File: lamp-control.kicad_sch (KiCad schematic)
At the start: 30 parts, among them J1 LED, J2 VIN, J3 Touch, J4 UART, J5 I²C, J6 SPI, Q1 BSS138, U1 ESP-12E, U2 AMS1117-3.3, U3 TTP223-BA6

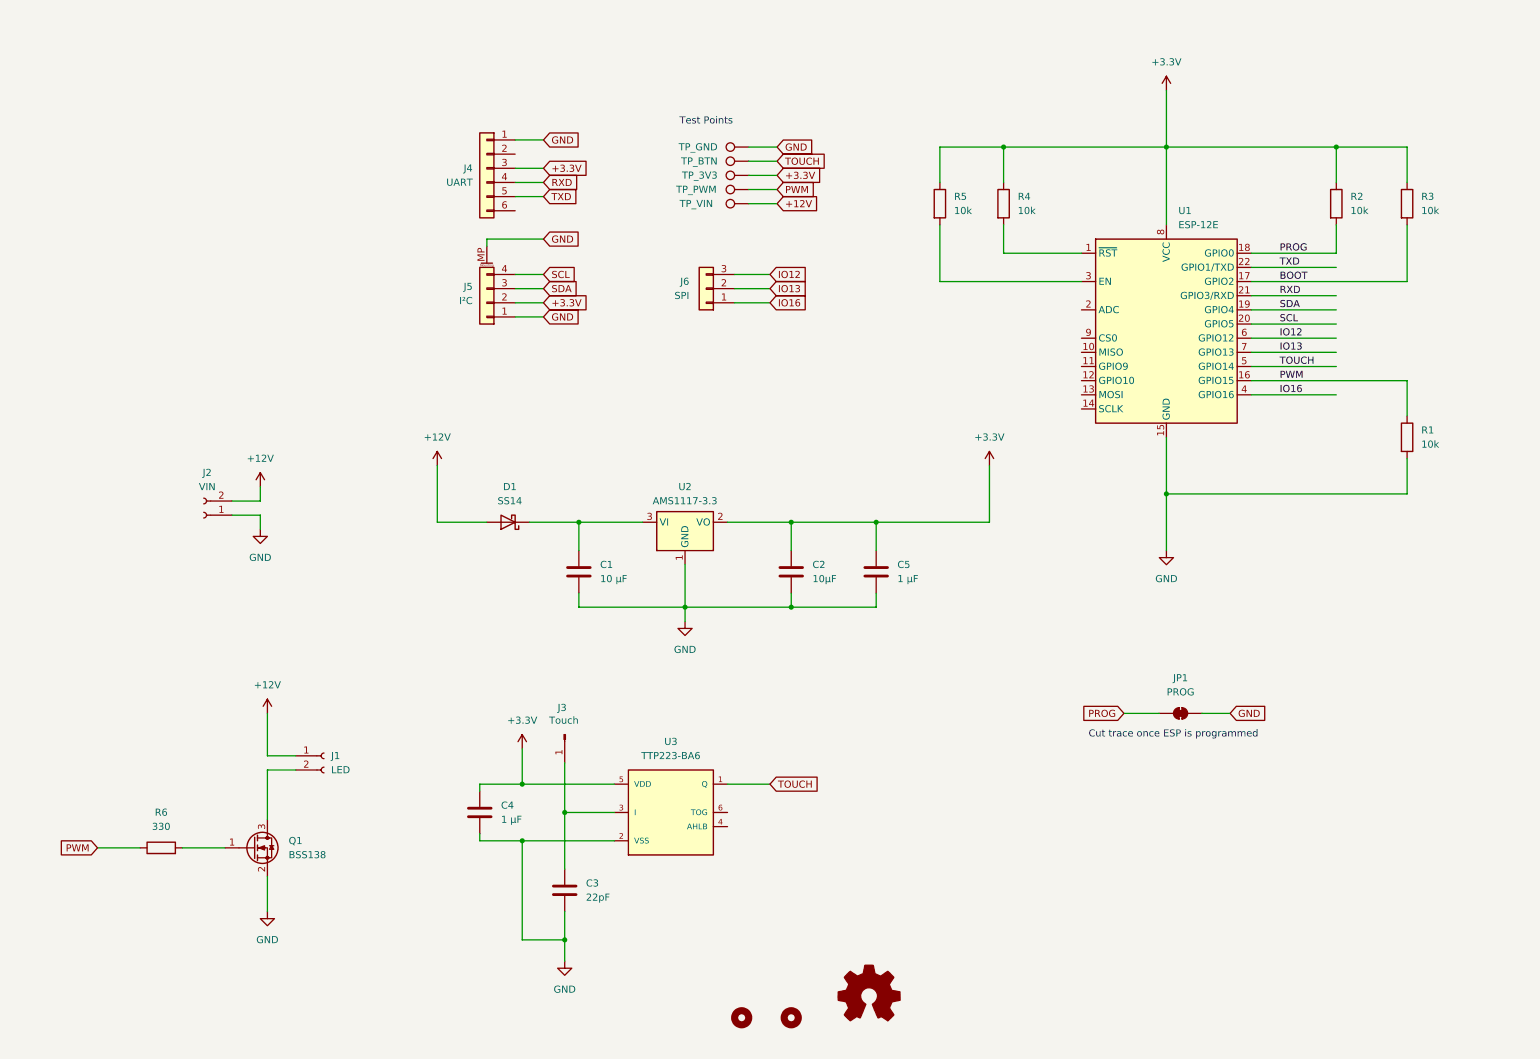
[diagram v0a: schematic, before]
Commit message: Simplify design (#1)
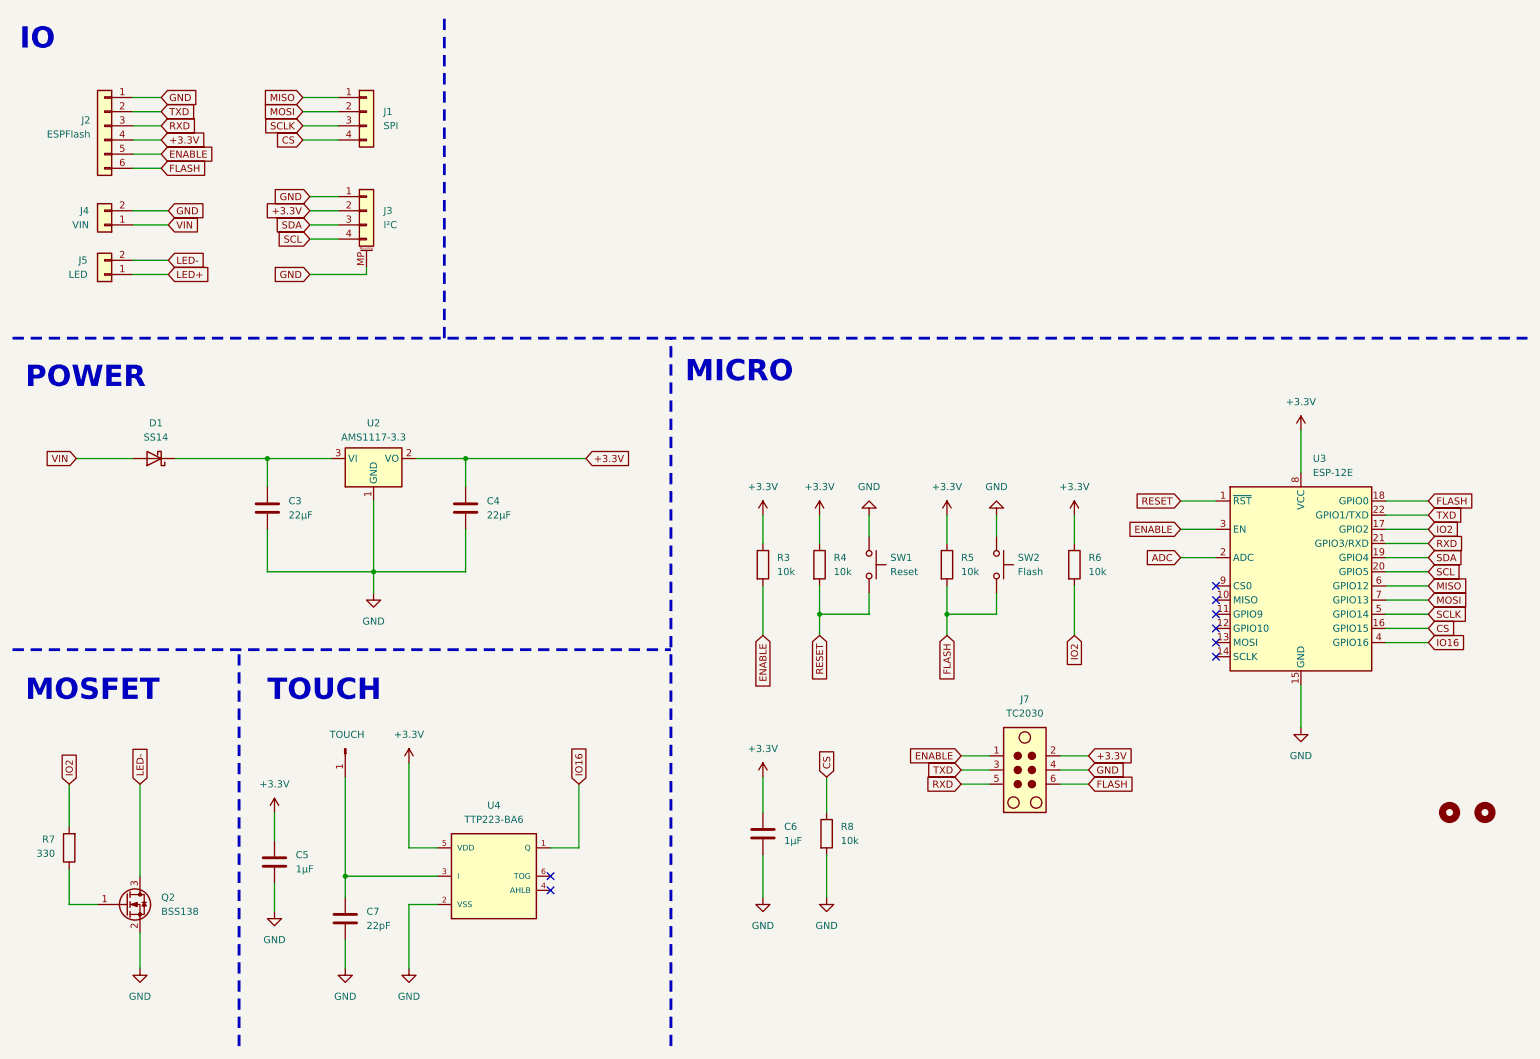
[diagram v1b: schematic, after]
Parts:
- removed C5: 1 µF, Capacitor_SMD:C_0805_2012Metric_Pad1.18x1.45mm_HandSolder, symbol Device:C
- removed JP1: PROG, Jumper:SolderJumper-2_P1.3mm_Bridged_RoundedPad1.0x1.5mm, symbol Jumper:SolderJumper_2_Bridged
- removed R2: 10k, Resistor_SMD:R_0805_2012Metric_Pad1.20x1.40mm_HandSolder, symbol Device:R
- removed TP1: TP_PWM, TestPoint:TestPoint_Pad_1.0x1.0mm, symbol Connector:TestPoint
- removed TP2: TP_BTN, TestPoint:TestPoint_Pad_1.0x1.0mm, symbol Connector:TestPoint
- removed TP3: TP_3V3, TestPoint:TestPoint_Pad_1.0x1.0mm, symbol Connector:TestPoint
- removed TP4: TP_GND, TestPoint:TestPoint_Pad_1.0x1.0mm, symbol Connector:TestPoint
- removed TP5: TP_VIN, TestPoint:TestPoint_Pad_1.0x1.0mm, symbol Connector:TestPoint
- added C6: 1µF, Capacitor_SMD:C_0805_2012Metric_Pad1.18x1.45mm_HandSolder, symbol Device:C
- added J7: TC2030, Connector:Tag-Connect_TC2030-IDC-NL_2x03_P1.27mm_Vertical, symbol Connector:TC2030
- added R6: 10k, Resistor_SMD:R_0805_2012Metric_Pad1.20x1.40mm_HandSolder, symbol Device:R
- added SW1: Reset, Button_Switch_SMD:SW_Tactile_SPST_NO_Straight_CK_PTS636Sx25SMTRLFS, symbol Switch:SW_Push
- added SW2: Flash, Button_Switch_SMD:SW_Tactile_SPST_NO_Straight_CK_PTS636Sx25SMTRLFS, symbol Switch:SW_Push
- C3: renamed from C1; value 10 µF -> 22µF; footprint Capacitor_SMD:C_0805_2012Metric_Pad1.18x1.45mm_HandSolder -> Capacitor_Tantalum_SMD:CP_EIA-3528-12_Kemet-T_HandSolder
- C4: renamed from C2; value 10µF -> 22µF; footprint Capacitor_SMD:C_0805_2012Metric_Pad1.18x1.45mm_HandSolder -> Capacitor_Tantalum_SMD:CP_EIA-3528-12_Kemet-T_HandSolder
- C5: renamed from C4; value 1 µF -> 1µF
- C7: renamed from C3; footprint Capacitor_SMD:C_0805_2012Metric_Pad1.18x1.45mm_HandSolder -> Capacitor_SMD:C_0603_1608Metric_Pad1.08x0.95mm_HandSolder
- J1: renamed from J6; footprint Connector_Wire:SolderWire-0.1sqmm_1x03_P3.6mm_D0.4mm_OD1mm -> Connector_PinHeader_2.54mm:PinHeader_1x04_P2.54mm_Horizontal; symbol Connector_Generic:Conn_01x03 -> Connector_Generic:Conn_01x04
- J2: renamed from J4; value UART -> ESPFlash; footprint Connector_PinHeader_2.54mm:PinHeader_1x06_P2.54mm_Vertical -> Connector_PinHeader_2.54mm:PinHeader_1x06_P2.54mm_Horizontal
- J4: renamed from J2; symbol Connector:Conn_01x02_Socket -> Connector_Generic:Conn_01x02; now in the parts list
- J5: renamed from J1; symbol Connector:Conn_01x02_Socket -> Connector_Generic:Conn_01x02; now in the parts list
- J6: renamed from J3; value Touch -> TOUCH
- renumbered J5 to J3, Q1 to Q2, R6 to R7, R1 to R8, U1 to U3, U3 to U4
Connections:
- net PROG is gone; now on net FLASH: U3.18 (GPIO0)
- net +3.3V: now also J2.4 (Pin_4), C6.1, J7.2, R6.1; no longer J2.3 (Pin_3)
- net GND: now also J4.2 (Pin_2), C6.2, J7.4, SW1.1, SW2.1; no longer J4.1 (Pin_1)
- net IO16: now also U4.1 (Q); no longer J1.1 (Pin_1)
- net RXD: now also J2.3 (Pin_3), J7.5; no longer J2.4 (Pin_4)
- net TXD: now also J2.2 (Pin_2), J7.3; no longer J2.5 (Pin_5)
- net at Q2.1 (G): now also R7.1; no longer R7.2
- net LED-: now reaches J5.2 (Pin_2), Q2.3 (D)
- net RESET: now reaches R4.2, U3.1 (~{RST})
- net RESET: now also SW1.2
- net ADC: now reaches U3.2 (ADC)
- net ENABLE: now reaches U3.3 (EN)
- net ENABLE: now also J2.5 (Pin_5), R3.2, J7.1; no longer R5.2
- net FLASH: now reaches J2.6 (Pin_6)
- net FLASH: now also R5.2, J7.6, SW2.2
- removed net +12V: D1.2 (A), J4.2 (Pin_2), J5.1 (Pin_1)
- net BOOT renamed IO2
- net IO2: now also R7.2, R6.2; no longer R3.2
- net IO12 renamed MISO
- net MISO: now also J1.1 (Pin_1); no longer J1.3 (Pin_3)
- net IO13 renamed MOSI
- net PWM renamed CS
- net CS: now also J1.4 (Pin_4); no longer R7.1
- net TOUCH renamed SCLK
- net SCLK: now also J1.3 (Pin_3); no longer U4.1 (Q)
- new net LED+: J5.1 (Pin_1)
- new net VIN: D1.2 (A), J4.1 (Pin_1)
- no-connect marks 0 -> 8
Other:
- note added: "IO"
- note added: "MICRO"
- note added: "MOSFET"
- note added: "POWER"
- note added: "TOUCH"
- note removed: "Cut trace once ESP is programmed"
- note removed: "Test Points"
- moved on the sheet: C3, C4, C5, C7, D1, J2, J3, J4, J5, Q2, R7, R8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
